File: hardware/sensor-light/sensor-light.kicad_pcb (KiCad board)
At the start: 2 copper layers, 95.2 x 33 mm, 14 parts, among them J2 PIR Sensor 2, J3 PIR Sensor 1, J4 PROG Header, J5 Light Sensor, J6 Power IN/OUT 12V, Q1 IRLML2502, SW1 Manual ON/OFF, U1 Reg 3.3V, U2 MSP430G2553IN20

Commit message: layout adjustments
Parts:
- added C2: 100nF, Capacitors_THT:C_Rect_L7.0mm_W2.5mm_P5.00mm, F.Cu at (129.5, 119.4)
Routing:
- net Net-(Q1-Pad1): track 68.3 -> 66.6 mm
- net Net-(R3-Pad1): track 28.0 -> 26.5 mm
- net Net-(J6-Pad2): track 15.5 -> 16.8 mm
- added copper zone on F.Cu, net (none)
- added copper zone on F.Cu, net Net-(J6-Pad2)
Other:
- net class Wide added: clearance 0.5, trace_width 1, via_dia 0.6, via_drill 0.4

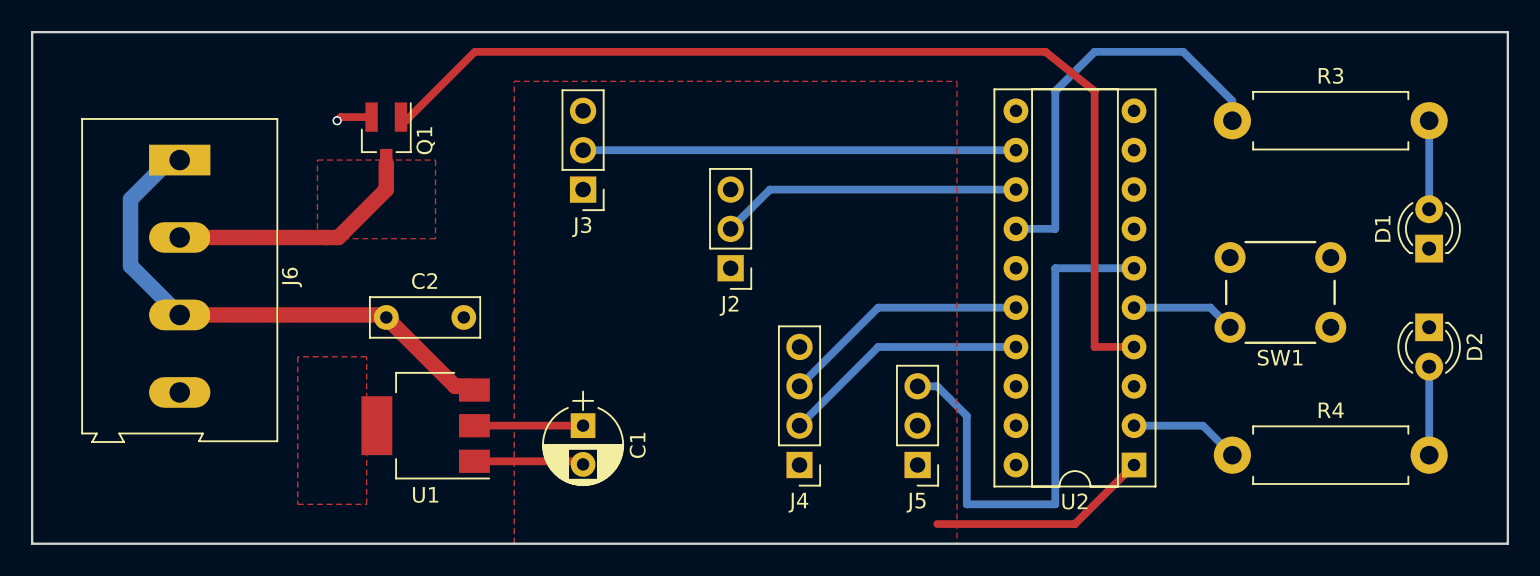
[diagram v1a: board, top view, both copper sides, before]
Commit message: some fiddling with thermal releif areas
Signed-off-by: Eugene Crosser <evgenii.cherkashin@profitbricks.com>
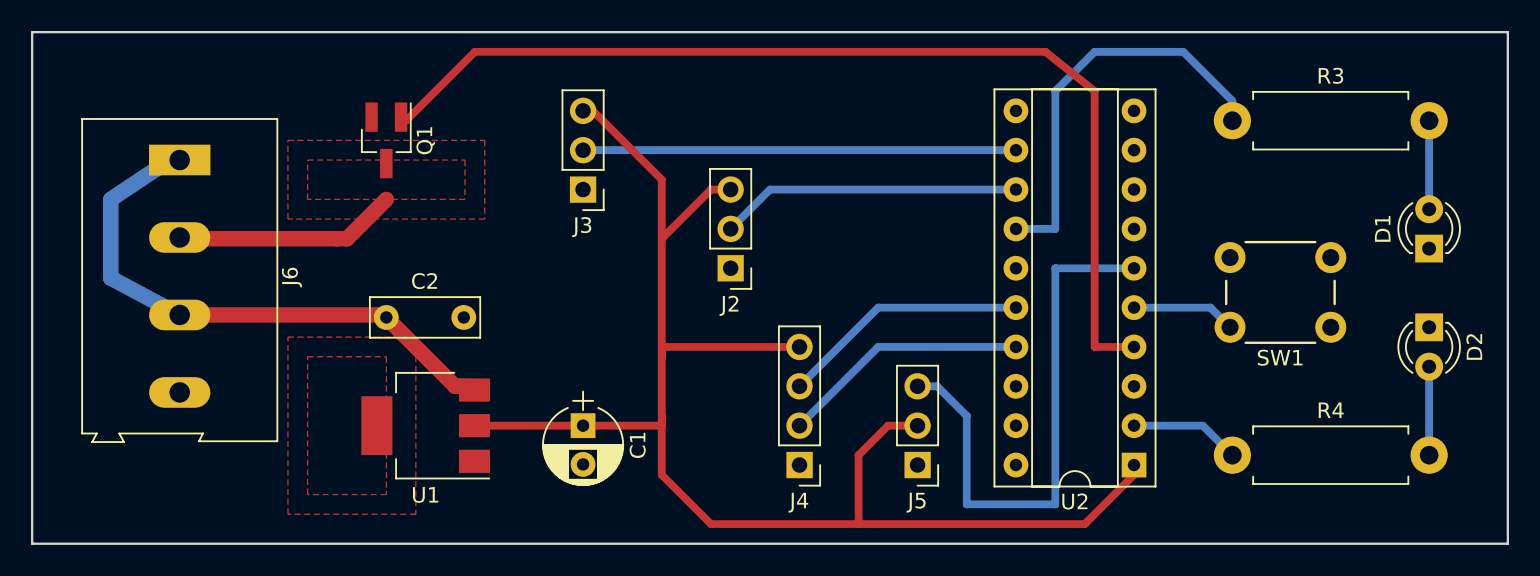
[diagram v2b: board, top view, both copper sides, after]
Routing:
- net Net-(C1-Pad1): track 21.3 -> 96.8 mm
- net Net-(C1-Pad2): track 9.41 -> 0.28 mm, vias 1 -> 0
- net Net-(C2-Pad1): track 34.3 -> 36.6 mm
- net Net-(J6-Pad2): track 16.8 -> 14.8 mm
- added copper zone on F.Cu, net Net-(C1-Pad2)
- added copper zone on F.Cu, net Net-(C2-Pad1)
- removed copper zone on F.Cu, net (none)
- removed copper zone on F.Cu, net Net-(C1-Pad1)

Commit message: redraw board, with correct releif areas
Signed-off-by: Eugene Crosser <evgenii.cherkashin@profitbricks.com>
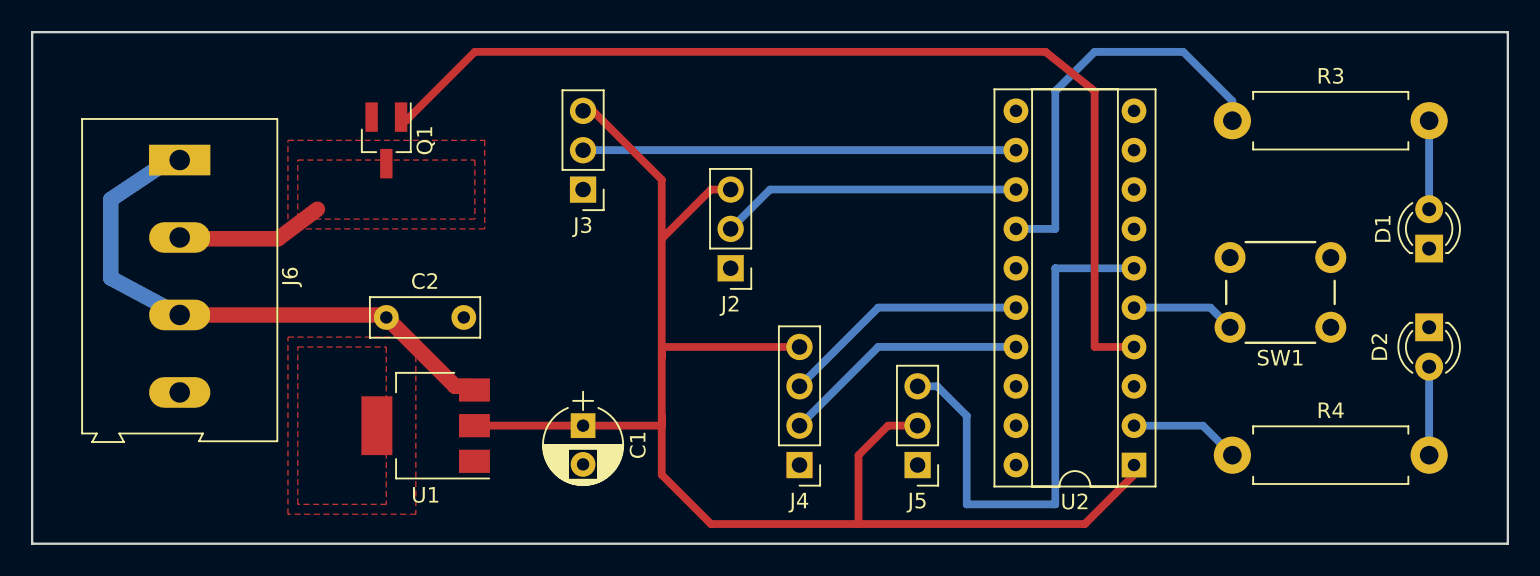
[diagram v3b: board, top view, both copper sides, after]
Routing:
- net Net-(J6-Pad2): track 14.8 -> 9.96 mm
- added copper zone on F.Cu, net Net-(C1-Pad1)
- removed copper zone on F.Cu, net Net-(C2-Pad1)
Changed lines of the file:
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@@
   (general
     (links 36)
-    (no_connects 3)
+    (no_connects 2)
     (area 106.604999 100.889999 202.005001 134.060001)
     (thickness 1.6)
@@
       (drillshape 0)
       (scaleselection 1)
-      (outputdirectory gerber/))
+      (outputdirectory ../))
   )
   (net 0 "")
@@
       (effects (font (size 1 1) (thickness 0.15)))
     )
-    (fp_text value Red (at 1.27 2.96 90) (layer F.Fab)
+    (fp_text value Red (at 1.27 3.175 90) (layer F.Fab)
       (effects (font (size 1 1) (thickness 0.15)))
     )
@@
     (descr "LED, diameter 3.0mm, 2 pins")
     (tags "LED diameter 3.0mm 2 pins")
-    (fp_text reference D2 (at 1.27 -2.96 270) (layer F.SilkS)
-      (effects (font (size 1 1) (thickness 0.15)))
-    )
-    (fp_text value Green (at 1.27 2.96 270) (layer F.Fab)
+    (fp_text reference D2 (at 1.27 3.175 270) (layer F.SilkS)
+      (effects (font (size 1 1) (thickness 0.15)))
+    )
+    (fp_text value Green (at 1.27 -3.175 270) (layer F.Fab)
       (effects (font (size 1 1) (thickness 0.15)))
     )
@@
       (effects (font (size 1 1) (thickness 0.15)))
     )
-    (fp_text value "Light Sensor" (at 0 7.41 180) (layer F.Fab)
+    (fp_text value "Light Sensor" (at 2.54 1.905 270) (layer F.Fab)
       (effects (font (size 1 1) (thickness 0.15)))
     )
@@
       (effects (font (size 1 1) (thickness 0.15)))
     )
-    (fp_text value IRLML2502 (at 0 2.5 270) (layer F.Fab)
+    (fp_text value IRLML2502 (at -4.445 1.27 360) (layer F.Fab)
       (effects (font (size 1 1) (thickness 0.15)))
     )
@@
       (effects (font (size 1 1) (thickness 0.15)))
     )
-    (fp_text value MSP430G2553IN20 (at 3.81 25.25 180) (layer F.Fab)
+    (fp_text value MSP430G2553IN20 (at 3.81 11.43 270) (layer F.Fab)
       (effects (font (size 1 1) (thickness 0.15)))
     )
@@
   (segment (start 167.005 131.445) (end 167.005 125.73) (width 0.5) (layer B.Cu) (net 12))
   (segment (start 164.465 123.825) (end 163.83 123.825) (width 0.5) (layer B.Cu) (net 12))
-  (segment (start 129.54 111.76) (end 127 114.3) (width 1) (layer F.Cu) (net 13))
-  (segment (start 126.365 114.3) (end 127 114.3) (width 1) (layer F.Cu) (net 13))
-  (segment (start 126.365 114.3) (end 116.285 114.3) (width 1) (layer F.Cu) (net 13))
+  (segment (start 125.095 112.395) (end 122.555 114.3) (width 1) (layer F.Cu) (net 13))
+  (segment (start 122.555 114.3) (end 122.555 114.3) (width 1) (layer F.Cu) (net 13))
+  (segment (start 122.555 114.3) (end 116.285 114.3) (width 1) (layer F.Cu) (net 13))
   (segment (start 116.285 114.3) (end 116.205 114.22) (width 1) (layer F.Cu) (net 13))
   (segment (start 129.54 109.45) (end 129.54 109.855) (width 0.5) (layer F.Cu) (net 13))
@@
   (segment (start 111.76 111.76) (end 111.76 116.84) (width 1) (layer B.Cu) (net 15))
   (segment (start 111.76 116.84) (end 116.205 119.22) (width 1) (layer B.Cu) (net 15))
-  (zone (net 15) (net_name "Net-(C2-Pad1)") (layer F.Cu) (hatch edge 0.508)
-    (connect_pads (clearance 0.508))
-    (min_thickness 0.254)
-    (fill yes (arc_segments 16) (thermal_gap 0.508) (thermal_bridge_width 0.508))
-    (polygon
-      (pts
-        (xy 129.54 130.81) (xy 124.46 130.81) (xy 124.46 121.92) (xy 129.54 121.92) (xy 129.54 130.81)
-      )
-    )
-  )
   (zone (net 13) (net_name "Net-(J6-Pad2)") (layer F.Cu) (hatch edge 0.508)
     (connect_pads (clearance 0.508))
@@
     (polygon
       (pts
-        (xy 134.62 111.76) (xy 124.46 111.76) (xy 124.46 109.22) (xy 134.62 109.22) (xy 134.62 111.76)
+        (xy 135.255 113.03) (xy 123.825 113.03) (xy 123.825 109.22) (xy 135.255 109.22)
       )
     )
@@
     )
     (polygon
-      (pts        (xy 123.19 107.95) (xy 135.89 107.95) (xy 135.89 113.03) (xy 123.19 113.03)
+      (pts        (xy 123.19 107.95) (xy 135.89 107.95) (xy 135.89 113.665) (xy 123.19 113.665)
       )
     )
@@
       )
     )
+  )
+  (zone (net 1) (net_name "Net-(C1-Pad1)") (layer F.Cu) (hatch edge 0.508)
+    (connect_pads (clearance 0.508))
+    (min_thickness 0.254)
+    (fill yes (arc_segments 16) (thermal_gap 0.508) (thermal_bridge_width 0.508))
+    (polygon
+      (pts
+        (xy 123.825 121.285) (xy 129.54 121.285) (xy 129.54 131.445) (xy 123.825 131.445)
+      )
+    )

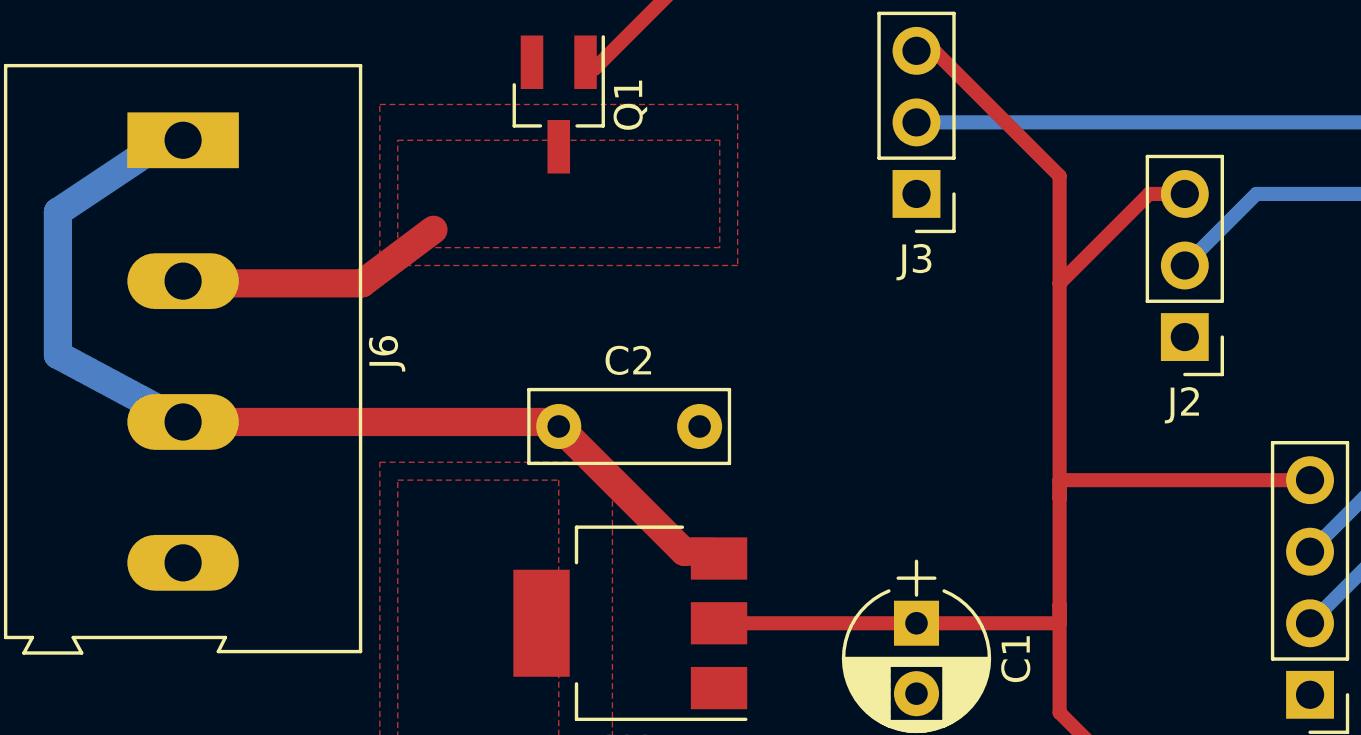
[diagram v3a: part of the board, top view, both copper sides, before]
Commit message: minor adjustment in traces and labels
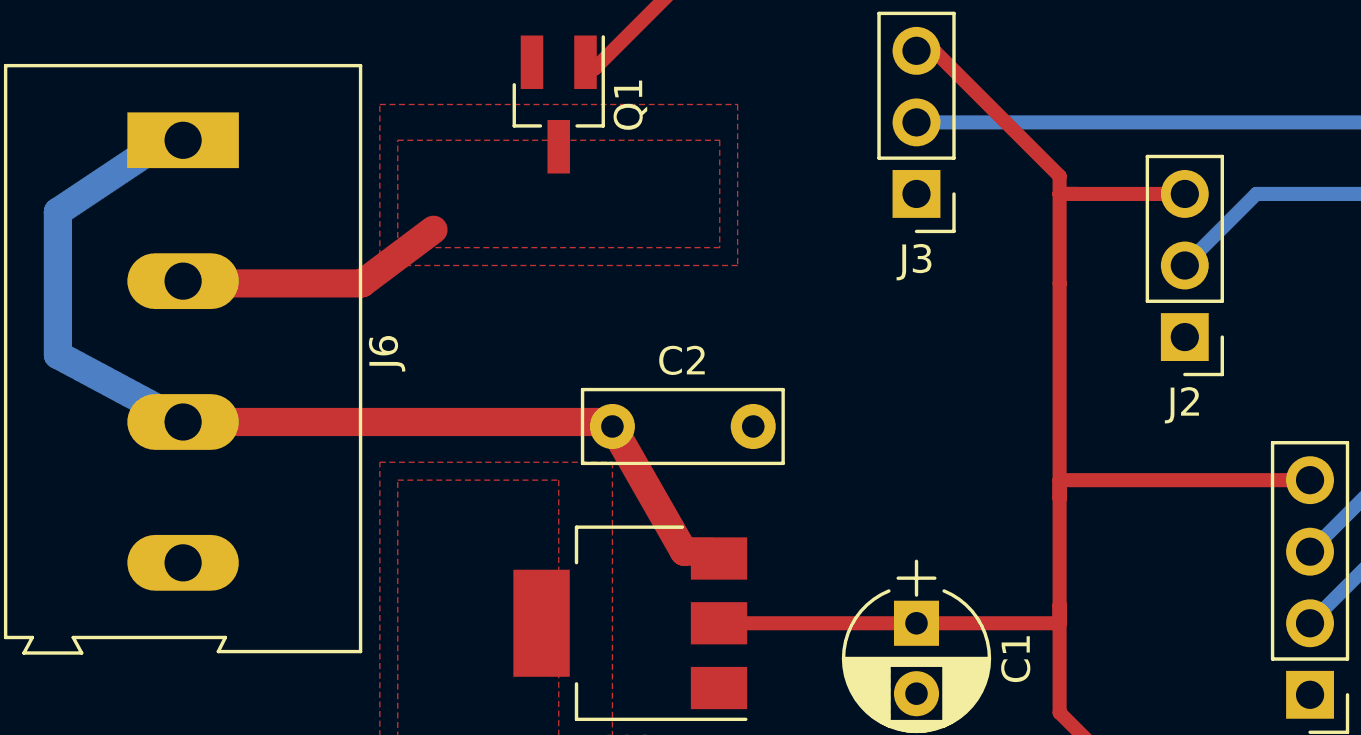
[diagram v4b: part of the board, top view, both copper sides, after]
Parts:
- C1: value 10uF -> 10μF
- R3: value 47Ω -> 47
- R4: value 27Ω -> 27
- moved C2 1.91 mm to (131.4, 119.4)
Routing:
- net Net-(C2-Pad1): track 36.6 -> 37.4 mm
- net Net-(C1-Pad1): track 96.8 -> 96.1 mm
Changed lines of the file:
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@@
-(kicad_pcb (version 4) (host pcbnew 4.0.2+dfsg1-stable)
+(kicad_pcb (version 4) (host pcbnew 4.0.6+dfsg1-1)
   (general
     (links 36)
@@
     (thickness 1.6)
     (drawings 4)
-    (tracks 69)
+    (tracks 71)
     (zones 0)
     (modules 15)
@@
       (drillshape 0)
       (scaleselection 1)
-      (outputdirectory ../))
+      (outputdirectory gerber/))
   )
   (net 0 "")
@@
       (effects (font (size 1 1) (thickness 0.15)))
     )
-    (fp_text value 10uF (at 5.715 0 360) (layer F.Fab)
+    (fp_text value 10μF (at 5.715 0 360) (layer F.Fab)
       (effects (font (size 1 1) (thickness 0.15)))
     )
@@
       (effects (font (size 1 1) (thickness 0.15)))
     )
-    (fp_text value 47Ω (at 6.35 2.86) (layer F.Fab)
+    (fp_text value 47 (at 6.35 2.86) (layer F.Fab)
       (effects (font (size 1 1) (thickness 0.15)))
     )
@@
       (effects (font (size 1 1) (thickness 0.15)))
     )
-    (fp_text value 27Ω (at 6.35 2.86) (layer F.Fab)
+    (fp_text value 27 (at 6.35 2.86) (layer F.Fab)
       (effects (font (size 1 1) (thickness 0.15)))
     )
@@
   )
   (module Capacitors_THT:C_Rect_L7.0mm_W2.5mm_P5.00mm (layer F.Cu)
-    (at 129.54 119.38)
+    (at 131.445 119.38)
     (descr "C, Rect series, Radial, pin pitch=5.00mm, , length*width=7*2.5mm^2, Capacitor")
     (tags "C Rect series Radial pin pitch 5.00mm  length 7mm width 2.5mm Capacitor")
@@
   (gr_line (start 201.93 100.965) (end 106.68 100.965) (angle 90) (layer Edge.Cuts) (width 0.15))
   (gr_line (start 201.93 133.985) (end 201.93 100.965) (angle 90) (layer Edge.Cuts) (width 0.15))
+  (segment (start 160.02 132.715) (end 160.02 128.27) (width 0.5) (layer F.Cu) (net 1))
+  (segment (start 147.32 110.49) (end 147.32 111.125) (width 0.5) (layer F.Cu) (net 1))
+  (segment (start 147.32 111.125) (end 147.955 111.125) (width 0.5) (layer F.Cu) (net 1))
+  (segment (start 151.765 111.125) (end 147.955 111.125) (width 0.5) (layer F.Cu) (net 1))
+  (segment (start 147.955 111.125) (end 147.32 111.125) (width 0.5) (layer F.Cu) (net 1))
   (segment (start 142.24 126.365) (end 135.23 126.365) (width 0.5) (layer F.Cu) (net 1))
   (segment (start 142.24 126.365) (end 147.32 126.365) (width 0.5) (layer F.Cu) (net 1))
   (segment (start 147.32 126.365) (end 147.32 125.73) (width 0.5) (layer F.Cu) (net 1))
-  (segment (start 160.02 132.715) (end 160.02 128.27) (width 0.5) (layer F.Cu) (net 1))
   (segment (start 161.925 126.365) (end 163.83 126.365) (width 0.5) (layer F.Cu) (net 1))
   (segment (start 160.02 128.27) (end 161.925 126.365) (width 0.5) (layer F.Cu) (net 1))
-  (segment (start 151.765 111.125) (end 150.495 111.125) (width 0.5) (layer F.Cu) (net 1))
-  (segment (start 150.495 111.125) (end 147.32 114.3) (width 0.5) (layer F.Cu) (net 1))
   (segment (start 156.21 121.285) (end 147.32 121.285) (width 0.5) (layer F.Cu) (net 1))
   (segment (start 147.32 121.285) (end 147.32 121.92) (width 0.5) (layer F.Cu) (net 1))
   (segment (start 160.02 132.715) (end 150.495 132.715) (width 0.5) (layer F.Cu) (net 1))
-  (segment (start 147.32 110.49) (end 147.32 114.3) (width 0.5) (layer F.Cu) (net 1))
+  (segment (start 147.32 111.125) (end 147.32 114.3) (width 0.5) (layer F.Cu) (net 1))
   (segment (start 147.32 114.3) (end 147.32 121.92) (width 0.5) (layer F.Cu) (net 1))
   (segment (start 147.32 121.92) (end 147.32 125.73) (width 0.5) (layer F.Cu) (net 1))
@@
   (segment (start 135.255 102.235) (end 130.81 106.68) (width 0.5) (layer F.Cu) (net 14))
   (segment (start 130.81 106.68) (end 130.49 106.45) (width 0.5) (layer F.Cu) (net 14))
-  (segment (start 129.54 119.38) (end 133.985 123.825) (width 1) (layer F.Cu) (net 15))
+  (segment (start 131.445 119.38) (end 133.985 123.825) (width 1) (layer F.Cu) (net 15) (status 400000))
   (segment (start 133.985 123.825) (end 134.99 123.825) (width 1) (layer F.Cu) (net 15))
   (segment (start 134.99 123.825) (end 135.23 124.065) (width 0.5) (layer F.Cu) (net 15))
-  (segment (start 116.205 119.22) (end 129.38 119.22) (width 1) (layer F.Cu) (net 15))
-  (segment (start 129.38 119.22) (end 129.54 119.38) (width 0.5) (layer F.Cu) (net 15))
+  (segment (start 116.205 119.22) (end 131.285 119.22) (width 1) (layer F.Cu) (net 15) (status 400000))
+  (segment (start 131.285 119.22) (end 131.445 119.38) (width 0.5) (layer F.Cu) (net 15) (status 800000))
   (segment (start 135.23 124.065) (end 135.23 123.8) (width 0.5) (layer F.Cu) (net 15))
   (segment (start 116.205 109.22) (end 115.57 109.22) (width 0.5) (layer B.Cu) (net 15))
